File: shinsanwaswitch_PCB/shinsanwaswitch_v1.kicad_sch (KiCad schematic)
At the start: 9 parts, among them J1 Conn_01x05_Male, Q1 2SC5395

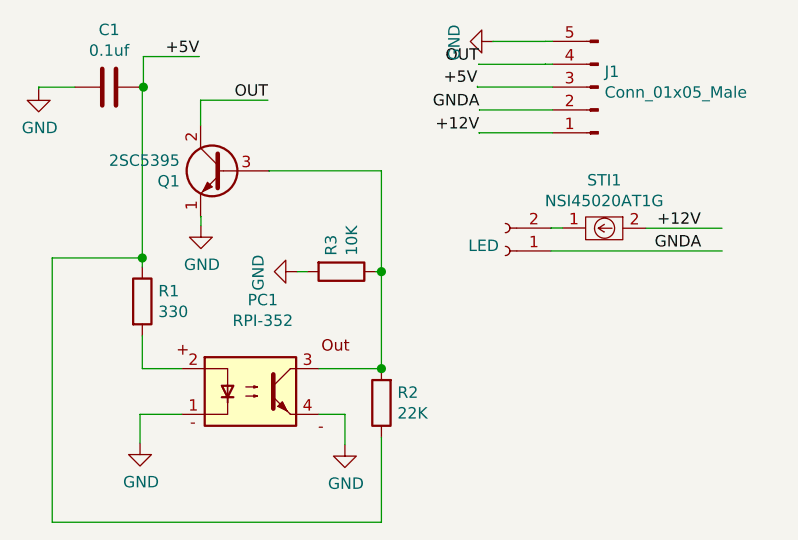
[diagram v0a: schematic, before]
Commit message: Update to Kicad 6.99 + RPI-352 footprint
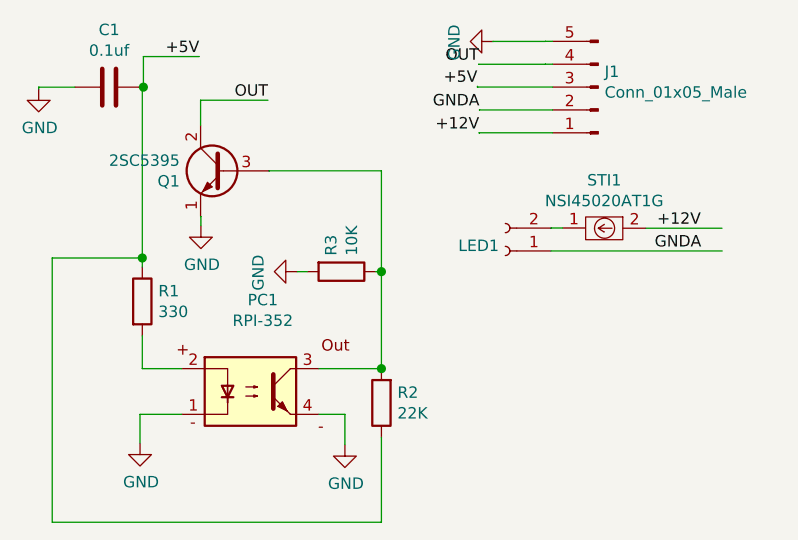
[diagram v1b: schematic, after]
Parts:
- renumbered LED to LED1
